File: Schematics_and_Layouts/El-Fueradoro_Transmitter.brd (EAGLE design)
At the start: 91.4 x 66 mm, 58 parts, among them IC1 MAX202, IC2 MEGA168P/328P, IC3 LM3940IT-3.3, Q1 9.8304

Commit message: Added bill of materials
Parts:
- R10, R11, R8, R9: value 1k8 -> 1k
- R12: value n.n. -> 3k9
- R13: value n.n. -> 6k8
- R14: value 4k7 -> 6k8
- R4, R5, R6: value 2k2 -> 1k
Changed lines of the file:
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@@
 <element name="C7" library="rcl" package="C025-024X044" value="100n" x="41.91" y="45.72"/>
 <element name="R1" library="rcl" package="0207/10" value="10k" x="43.18" y="50.8" rot="R180"/>
-<element name="R4" library="rcl" package="0207/10" value="2k2" x="76.2" y="15.24"/>
-<element name="R5" library="rcl" package="0207/10" value="2k2" x="76.2" y="12.7"/>
-<element name="R6" library="rcl" package="0207/10" value="2k2" x="76.2" y="10.16"/>
+<element name="R4" library="rcl" package="0207/10" value="1k" x="76.2" y="15.24"/>
+<element name="R5" library="rcl" package="0207/10" value="1k" x="76.2" y="12.7"/>
+<element name="R6" library="rcl" package="0207/10" value="1k" x="76.2" y="10.16"/>
 <element name="R2" library="rcl" package="0207/10" value="10k" x="78.74" y="55.88" rot="R270"/>
 <element name="R3" library="rcl" package="0207/10" value="10k" x="71.12" y="55.88" rot="R90"/>
@@
 <element name="C8" library="rcl" package="C025-024X044" value="15p" x="26.67" y="17.78"/>
 <element name="C9" library="rcl" package="C025-024X044" value="15p" x="26.67" y="15.24"/>
-<element name="R8" library="rcl" package="0207/10" value="1k8" x="22.86" y="5.08"/>
-<element name="R9" library="rcl" package="0207/10" value="1k8" x="22.86" y="7.62"/>
-<element name="R10" library="rcl" package="0207/10" value="1k8" x="22.86" y="10.16"/>
-<element name="R11" library="rcl" package="0207/10" value="1k8" x="22.86" y="12.7"/>
+<element name="R8" library="rcl" package="0207/10" value="1k" x="22.86" y="5.08"/>
+<element name="R9" library="rcl" package="0207/10" value="1k" x="22.86" y="7.62"/>
+<element name="R10" library="rcl" package="0207/10" value="1k" x="22.86" y="10.16"/>
+<element name="R11" library="rcl" package="0207/10" value="1k" x="22.86" y="12.7"/>
 <element name="LED_O" library="led" package="LED5MM" value="" x="11.43" y="15.24" smashed="yes" rot="R180">
 <attribute name="NAME" x="15.875" y="13.4366" size="1.27" layer="25" ratio="10" rot="R180"/>
@@
 <element name="DB7" library="solpad" package="LSP10" value="LSP10" x="50.8" y="25.4"/>
 <element name="RS" library="solpad" package="LSP10" value="LSP10" x="50.8" y="40.64"/>
-<element name="R12" library="rcl" package="0207/10" value="n.n." x="55.88" y="38.1" rot="R90"/>
-<element name="R13" library="rcl" package="0207/10" value="n.n." x="27.94" y="27.94" rot="R180"/>
+<element name="R12" library="rcl" package="0207/10" value="3k9" x="55.88" y="38.1" rot="R90"/>
+<element name="R13" library="rcl" package="0207/10" value="6k8" x="27.94" y="27.94" rot="R180"/>
 <element name="LCD_VCC" library="solpad" package="LSP10" value="LSP10" x="50.8" y="45.72"/>
 <element name="LCD_CONTR" library="solpad" package="LSP10" value="LSP10" x="50.8" y="43.18"/>
@@
 <element name="C11" library="rcl" package="B45181A" value="100u" x="6.35" y="29.21" rot="R90"/>
 <element name="U$2" library="fp" package="TO92-LINE" value="DS18B20" x="80.01" y="5.08" rot="R90"/>
-<element name="R14" library="rcl" package="0207/10" value="4k7" x="58.42" y="3.81" rot="R345.9"/>
+<element name="R14" library="rcl" package="0207/10" value="6k8" x="58.42" y="3.81" rot="R345.9"/>
 <element name="U$3" library="fp" package="RFM69CW" value="RFM69CW" x="76.2" y="33.02" rot="R270"/>
 </elements>

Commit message: Added size-information-output for Hexfiles/build_hexfiles.bat Extended manual and added BOMs BOM-Update (final one, hopefully!)
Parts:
- C14: value (none) -> 10u
- R12: value 3k9 -> 3k3
- R14: value 6k8 -> 3k3
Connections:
- net +5V renamed +3V3
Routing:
- net +3V3: track 251.7 -> 248.1 mm

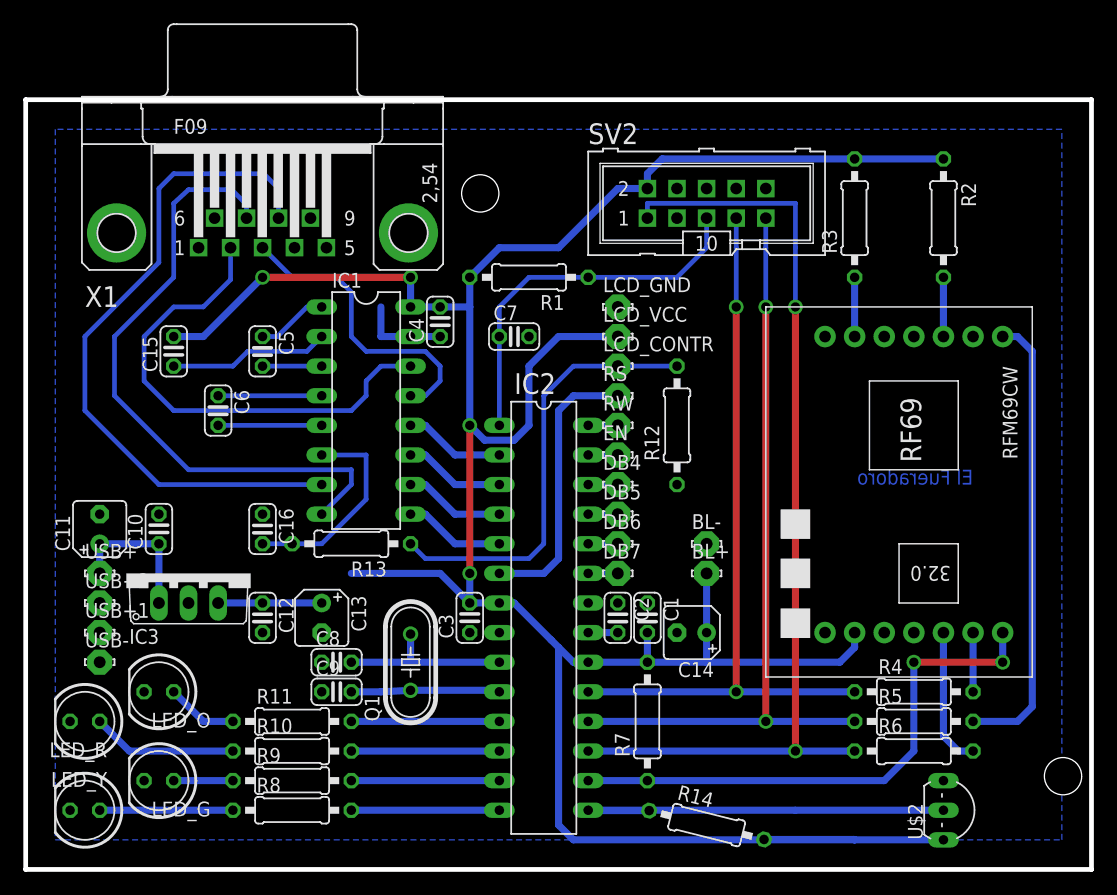
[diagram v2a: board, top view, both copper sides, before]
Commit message: Layout fixes Additions to manual once again
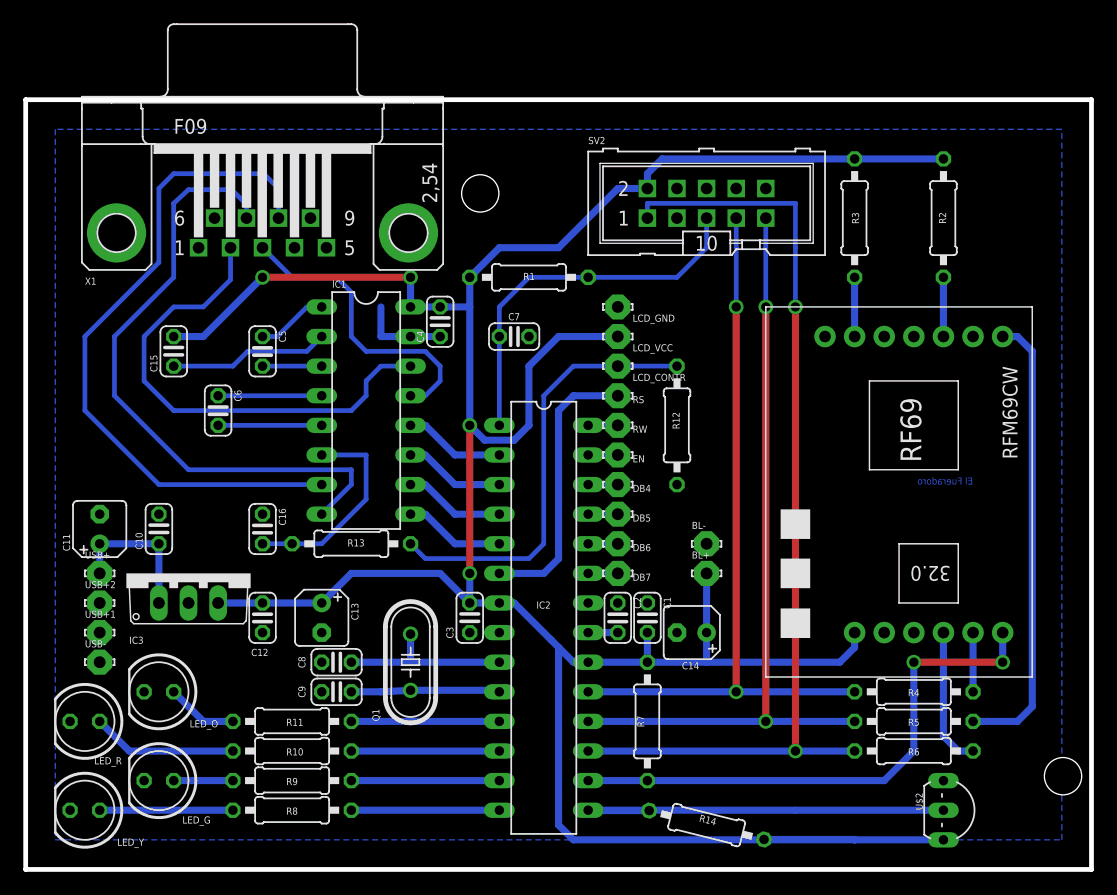
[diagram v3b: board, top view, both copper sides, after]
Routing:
- net +3V3: track 248.1 -> 251.7 mm

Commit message: Added Gerber Files
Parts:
- renumbered USB+ to +5V, USB+1 to D+, USB+2 to D-, USB- to GND
